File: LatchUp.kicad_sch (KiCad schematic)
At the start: 26 parts, among them Q10 IRF7406, Q11 BSL307SP, Q9 BSS138, U25 INA138NA_3K, U26 AD589JRZ, U27 LT1636CMS8_PBF

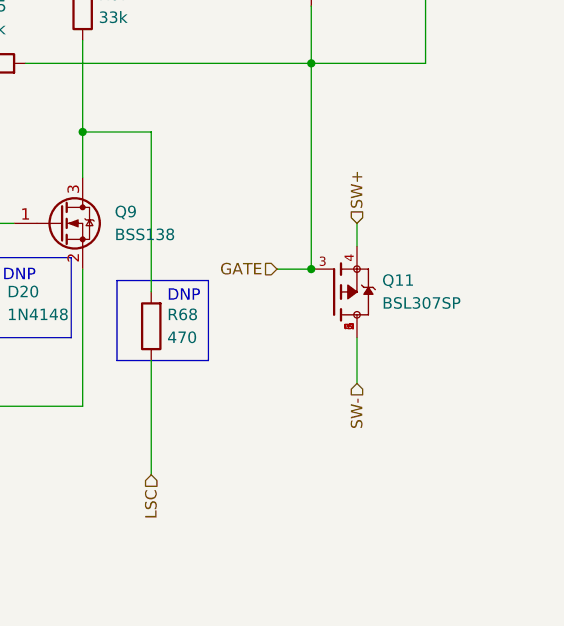
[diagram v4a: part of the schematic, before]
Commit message: Add a couple of Zener diodes to protect inputs of MOSFETs
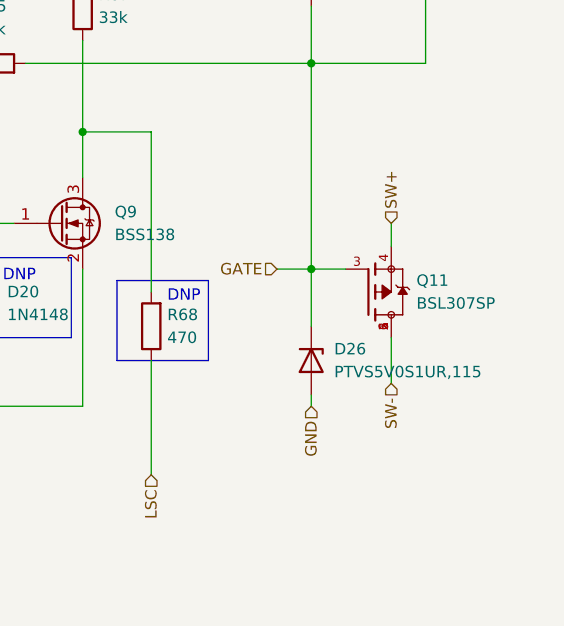
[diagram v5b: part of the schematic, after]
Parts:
- added D26: PTVS5V0S1UR,115, Diode_SMD:D_SOD-123, symbol Device:D_Zener
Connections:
- net GATE: now also D26.1 (K)
- net GND: now also D26.2 (A)
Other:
- moved on the sheet: Q11
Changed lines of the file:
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@@
     (stroke (width 0) (type default) (color 0 0 0 0))
   )
-  (wire (pts (xy 256.54 104.14) (xy 256.54 109.22))
+  (wire (pts (xy 260.35 104.14) (xy 260.35 109.22))
     (stroke (width 0) (type default) (color 0 0 0 0))
   )
@@
     (stroke (width 0) (type default) (color 0 0 0 0))
   )
+  (wire (pts (xy 251.46 96.52) (xy 251.46 102.87))
+    (stroke (width 0) (type default) (color 0 0 0 0))
+  )
   (wire (pts (xy 226.06 60.96) (xy 226.06 62.23))
     (stroke (width 0) (type default) (color 0 0 0 0))
@@
     (stroke (width 0) (type default) (color 0 0 0 0))
   )
-  (wire (pts (xy 256.54 91.44) (xy 256.54 93.98))
+  (wire (pts (xy 260.35 91.44) (xy 260.35 93.98))
     (stroke (width 0) (type default) (color 0 0 0 0))
   )
@@
     (stroke (width 0) (type default) (color 0 0 0 0))
   )
+  (wire (pts (xy 255.27 96.52) (xy 251.46 96.52))
+    (stroke (width 0) (type default) (color 0 0 0 0))
+  )
   (wire (pts (xy 233.68 99.06) (xy 233.68 81.28))
     (stroke (width 0) (type default) (color 0 0 0 0))
@@
   )
   (wire (pts (xy 88.9 95.25) (xy 96.52 95.25))
+    (stroke (width 0) (type default) (color 0 0 0 0))
+  )
+  (wire (pts (xy 251.46 110.49) (xy 251.46 111.76))
     (stroke (width 0) (type default) (color 0 0 0 0))
   )
@@
     (effects (font (size 1.27 1.27)) (justify right))
   )
-  (hierarchical_label "SW+" (shape input) (at 256.54 91.44 90)
+  (hierarchical_label "SW+" (shape input) (at 260.35 91.44 90)
     (effects (font (size 1.27 1.27)) (justify left))
   )
@@
   )
   (hierarchical_label "CT0" (shape input) (at 189.23 119.38 270)
+    (effects (font (size 1.27 1.27)) (justify right))
+  )
+  (hierarchical_label "GND" (shape input) (at 251.46 111.76 270)
     (effects (font (size 1.27 1.27)) (justify right))
   )
@@
     (effects (font (size 1.27 1.27)) (justify left))
   )
-  (hierarchical_label "SW-" (shape input) (at 256.54 109.22 270)
+  (hierarchical_label "SW-" (shape input) (at 260.35 109.22 270)
     (effects (font (size 1.27 1.27)) (justify right))
   )
@@
     (pin "4")
     (pin "5")
+  )
+  (symbol (lib_id "Device:D_Zener") (at 251.46 106.68 270) (unit 1)
+    (in_bom yes) (on_board yes) (fields_autoplaced)
+    (property "Reference" "D26" (id 0) (at 254 105.4099 90)
+      (effects (font (size 1.27 1.27)) (justify left))
+    )
+    (property "Value" "PTVS5V0S1UR,115 " (id 1) (at 254 107.9499 90)
+      (effects (font (size 0 0)) (justify left))
+    )
+    (property "Footprint" "Diode_SMD:D_SOD-123" (id 2) (at 251.46 106.68 0)
+      (effects (font (size 1.27 1.27)) hide)
+    )
+    (property "Datasheet" "~" (id 3) (at 251.46 106.68 0)
+      (effects (font (size 1.27 1.27)) hide)
+    )
+    (property "JLCPCB Part #" "C478011" (id 4) (at 251.46 106.68 0)
+      (effects (font (size 1.27 1.27)) hide)
+    )
+    (property "Manufacturer_Part_Number" "PTVS5V0S1UR,115 " (id 5) (at 251.46 106.68 0)
+      (effects (font (size 1.27 1.27)) hide)
+    )
+    (pin "1")
+    (pin "2")
   )
   (symbol (lib_id "Diode:BZX84Cxx") (at 234.95 57.15 270) (unit 1)
@@
     (pin "2")
   )
-  (symbol (lib_id "STS1_COBC_V2-rescue:BSL307SP") (at 254 99.06 0) (unit 1)
-    (in_bom yes) (on_board yes) (fields_autoplaced)
-    (property "Reference" "Q11" (id 0) (at 259.334 97.7899 0)
-      (effects (font (size 1.27 1.27)) (justify left))
-    )
-    (property "Value" "BSL307SP" (id 1) (at 259.334 100.3299 0)
-      (effects (font (size 1.27 1.27)) (justify left))
-    )
-    (property "Footprint" "Package_SO:TSOP-6_1.65x3.05mm_P0.95mm" (id 2) (at 257.81 71.12 0)
-      (effects (font (size 1.27 1.27)) (justify bottom) hide)
-    )
-    (property "Datasheet" "" (id 3) (at 254 99.06 0)
-      (effects (font (size 1.27 1.27)) hide)
-    )
-    (property "MF" "Infineon Technologies" (id 4) (at 232.41 71.12 0)
-      (effects (font (size 1.27 1.27)) (justify bottom) hide)
-    )
-    (property "Description" "P-Channel 30 V 5.5A (Ta) 2W (Ta) Surface Mount PG-TSOP-6-1" (id 5) (at 254 99.06 0)
-      (effects (font (size 1.27 1.27)) (justify bottom) hide)
-    )
-    (property "Package" "TSOT-23-6 Infineon" (id 6) (at 254 121.92 0)
-      (effects (font (size 1.27 1.27)) (justify bottom) hide)
-    )
-    (property "Price" "None" (id 7) (at 252.73 127 0)
-      (effects (font (size 1.27 1.27)) (justify bottom) hide)
-    )
-    (property "SnapEDA_Link" "https://www.snapeda.com/parts/BSL307SP/Infineon+Technologies/view-part/?ref=snap" (id 8) (at 254 119.38 0)
-      (effects (font (size 1.27 1.27)) (justify bottom) hide)
-    )
-    (property "MP" "BSL307SP" (id 9) (at 259.08 83.82 0)
-      (effects (font (size 1.27 1.27)) (justify bottom) hide)
-    )
-    (property "Purchase-URL" "https://www.snapeda.com/api/url_track_click_mouser/?unipart_id=578225&manufacturer=Infineon Technologies&part_name=BSL307SP&search_term=None" (id 10) (at 254 113.03 0)
-      (effects (font (size 1.27 1.27)) (justify bottom) hide)
-    )
-    (property "Availability" "In Stock" (id 11) (at 254 124.46 0)
-      (effects (font (size 1.27 1.27)) (justify bottom) hide)
-    )
-    (property "Check_prices" "https://www.snapeda.com/parts/BSL307SP/Infineon+Technologies/view-part/?ref=eda" (id 12) (at 254 115.57 0)
-      (effects (font (size 1.27 1.27)) (justify bottom) hide)
-    )
-    (property "Manufacturer_Part_Number" "BSL307SP H6327" (id 13) (at 254 99.06 0)
-      (effects (font (size 1.27 1.27)) hide)
-    )
-    (property "JLCPCB Part #" "C534457" (id 14) (at 254 99.06 0)
-      (effects (font (size 1.27 1.27)) hide)
-    )
+  (symbol (lib_id "STS1_COBC_V2-rescue:BSL307SP") (at 257.81 99.06 0) (unit 1)
+    (in_bom yes) (on_board yes) (fields_autoplaced)
+    (property "Reference" "Q11" (id 0) (at 263.144 97.7899 0)
+      (effects (font (size 1.27 1.27)) (justify left))
+    )
+    (property "Value" "BSL307SP" (id 1) (at 263.144 100.3299 0)
+      (effects (font (size 1.27 1.27)) (justify left))
+    )
+    (property "Footprint" "Package_SO:TSOP-6_1.65x3.05mm_P0.95mm" (id 2) (at 261.62 71.12 0)
+      (effects (font (size 1.27 1.27)) (justify bottom) hide)
+    )
+    (property "Datasheet" "" (id 3) (at 257.81 99.06 0)
+      (effects (font (size 1.27 1.27)) hide)
+    )
+    (property "MF" "Infineon Technologies" (id 4) (at 236.22 71.12 0)
+      (effects (font (size 1.27 1.27)) (justify bottom) hide)
+    )
+    (property "Description" "P-Channel 30 V 5.5A (Ta) 2W (Ta) Surface Mount PG-TSOP-6-1" (id 5) (at 257.81 99.06 0)
+      (effects (font (size 1.27 1.27)) (justify bottom) hide)
+    )
+    (property "Package" "TSOT-23-6 Infineon" (id 6) (at 257.81 121.92 0)
+      (effects (font (size 1.27 1.27)) (justify bottom) hide)
+    )
+    (property "Price" "None" (id 7) (at 256.54 127 0)
+      (effects (font (size 1.27 1.27)) (justify bottom) hide)
+    )
+    (property "SnapEDA_Link" "https://www.snapeda.com/parts/BSL307SP/Infineon+Technologies/view-part/?ref=snap" (id 8) (at 257.81 119.38 0)
+      (effects (font (size 1.27 1.27)) (justify bottom) hide)
+    )
+    (property "MP" "BSL307SP" (id 9) (at 262.89 83.82 0)
+      (effects (font (size 1.27 1.27)) (justify bottom) hide)
+    )
+    (property "Purchase-URL" "https://www.snapeda.com/api/url_track_click_mouser/?unipart_id=578225&manufacturer=Infineon Technologies&part_name=BSL307SP&search_term=None" (id 10) (at 257.81 113.03 0)
+      (effects (font (size 1.27 1.27)) (justify bottom) hide)
+    )
+    (property "Availability" "In Stock" (id 11) (at 257.81 124.46 0)
+      (effects (font (size 1.27 1.27)) (justify bottom) hide)
+    )
+    (property "Check_prices" "https://www.snapeda.com/parts/BSL307SP/Infineon+Technologies/view-part/?ref=eda" (id 12) (at 257.81 115.57 0)
+      (effects (font (size 1.27 1.27)) (justify bottom) hide)
+    )
+    (property "Manufacturer_Part_Number" "BSL307SP H6327" (id 13) (at 257.81 99.06 0)
+      (effects (font (size 1.27 1.27)) hide)
+    )
+    (property "JLCPCB Part #" "C534457" (id 14) (at 257.81 99.06 0)
+      (effects (font (size 1.27 1.27)) hide)
+    )

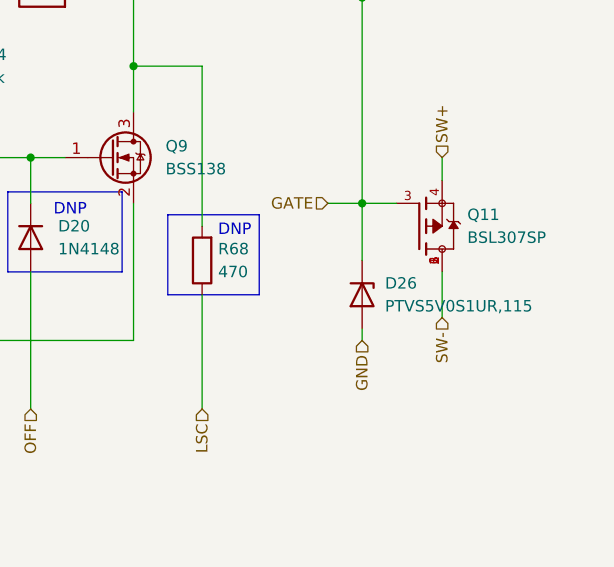
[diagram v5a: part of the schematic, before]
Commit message: Fix power domain crossing issue between RF and STM units
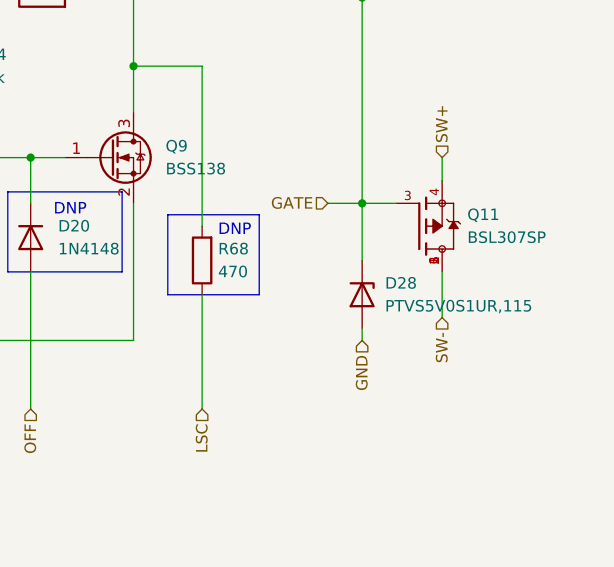
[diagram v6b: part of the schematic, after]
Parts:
- renumbered D26 to D28
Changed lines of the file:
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@@
   (symbol (lib_id "Device:D_Zener") (at 251.46 106.68 270) (unit 1)
     (in_bom yes) (on_board yes) (fields_autoplaced)
-    (property "Reference" "D26" (id 0) (at 254 105.4099 90)
+    (property "Reference" "D28" (id 0) (at 254 105.4099 90)
       (effects (font (size 1.27 1.27)) (justify left))
     )

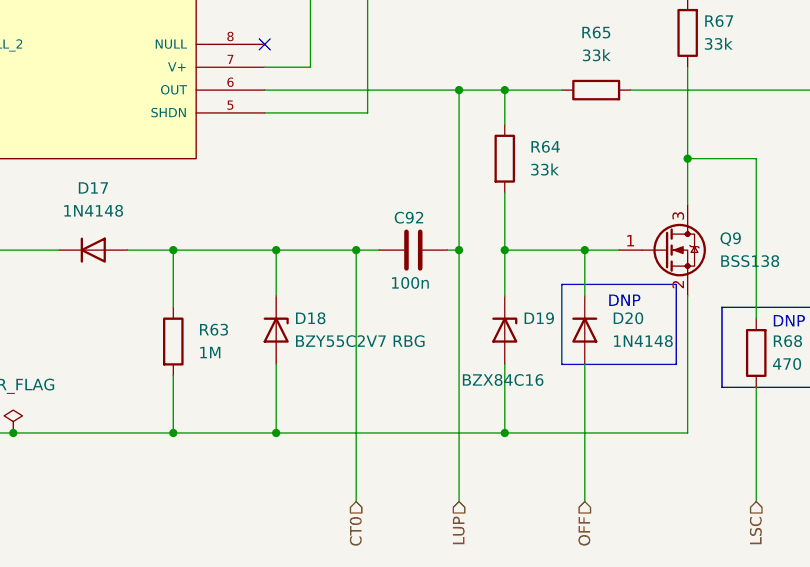
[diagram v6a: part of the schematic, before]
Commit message: Increase latch-up protection recovery time from ~10 ms to ~100 ms and add some GND vias to connect disconnected parts for In1.Cu layer
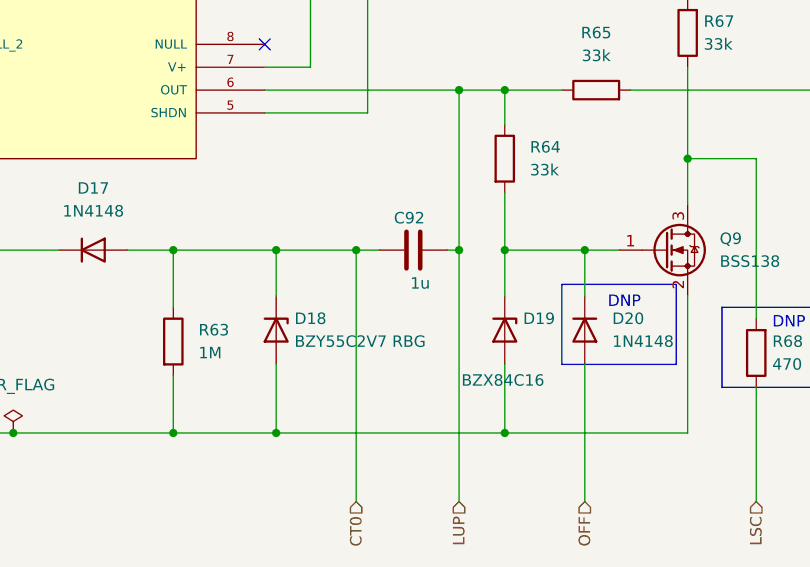
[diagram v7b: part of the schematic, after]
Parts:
- C92: value 100n -> 1u; JLCPCB Part # C1591 -> C307479; Manufacturer_Part_Number CL10B104KB8NNNC -> CL10B105KA8NFNC
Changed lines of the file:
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@@
       (effects (font (size 1.27 1.27)) (justify right))
     )
-    (property "Value" "100n" (id 1) (at 197.4472 95.1308 90)
+    (property "Value" "1u" (id 1) (at 197.4472 95.1308 90)
       (effects (font (size 1.27 1.27)) (justify right))
     )
@@
       (effects (font (size 1.27 1.27)) hide)
     )
-    (property "JLCPCB Part #" "C1591" (id 4) (at 195.58 91.44 0)
+    (property "JLCPCB Part #" "C307479" (id 4) (at 195.58 91.44 0)
       (effects (font (size 1.27 1.27)) hide)
     )
-    (property "Manufacturer_Part_Number" "CL10B104KB8NNNC " (id 5) (at 195.58 91.44 0)
+    (property "Manufacturer_Part_Number" "CL10B105KA8NFNC " (id 5) (at 195.58 91.44 0)
       (effects (font (size 1.27 1.27)) hide)
     )
